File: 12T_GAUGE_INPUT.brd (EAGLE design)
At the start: 160 x 100 mm, 102 parts, among them J1 MICRO-SD_CARD_SOCKET, P1_WP_PULLUP 10k, P2_WP_PULLUP 10k, P3_WP_PULLUP 10k, U15 WS2812

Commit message: Routed board
Not optimized for size. This is a POC to get an idea of what the minimum size of the board can be
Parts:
- removed 3V-R1: 240, rcl:R1206
- removed 3V-R2: 390, rcl:R1206
- removed 3V3-DCPL: 10uF, rcl:C1206
- removed 3VREG: V_REG_317SMD, SparkFun-IC-Power:SOT223
- removed U15: WS2812, SparkFun-LED:LED-TRICOLOR-5050-IC
- added CAL12: WS2812, SparkFun-LED:LED-TRICOLOR-5050-IC
- added RTC_DCPL: 22uF, rcl:C1206
- moved CAL4 173.5 mm to (74.9, 11.4)
- moved B3-R1 166.0 mm to (58.4, 7.62), flipped to the bottom, turned to 90 degrees
- moved GAUGE2 163.2 mm to (47.0, 2.54)
- moved ADS2 156.8 mm to (69.8, 43.2), flipped to the bottom, turned to 270 degrees
- moved B7-R2 156.4 mm to (74.9, 53.3), flipped to the bottom, turned to 270 degrees
- moved B8-R2 156.4 mm to (59.7, 53.3), flipped to the bottom, turned to 270 degrees
- moved ADS2-DCPL2 155.7 mm to (61.0, 41.9), flipped to the bottom
- moved GAUGE6 154.0 mm to (90.2, 39.4), turned to 270 degrees
- moved B8-R1 153.9 mm to (64.8, 53.3), flipped to the bottom, turned to 270 degrees
- moved B6-R2 152.8 mm to (83.8, 41.9), flipped to the bottom, turned to 180 degrees
- moved B7-R1 152.7 mm to (78.7, 53.3), flipped to the bottom, turned to 270 degrees
- moved CAL3 152.0 mm to (61.0, 11.4)
- moved POT1-DCPL 151.0 mm to (58.4, 30.5)
- moved B2-R2 150.0 mm to (48.3, 7.62), flipped to the bottom, turned to 90 degrees
- moved GAUGE5 149.4 mm to (90.2, 25.4), turned to 270 degrees
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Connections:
- removed net +3V3: 3V-R1.2, 3V3-DCPL.1, 3VREG.2
- removed net N$8: 3V-R1.1, 3V-R2.2, 3VREG.1
- net +12V: no longer 3VREG.3
- net +5V: now also CAL12.3, CAL12.5, RTC_DCPL.1; no longer U15.3, U15.5
- net GND: now also CAL12.6, RTC_DCPL.2; no longer 3V-R2.1, 3V3-DCPL.2, U15.6
- net N$17: now also CAL12.2; no longer U15.2
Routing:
- net +5V: track 0.00 -> 558.2 mm, vias 0 -> 17
- net GND: track 0.00 -> 496.4 mm, vias 0 -> 31
- net AGND: track 0.00 -> 439.3 mm, vias 0 -> 10
- net V+: track 0.00 -> 362.9 mm, vias 0 -> 3
- net MOSI: track 0.00 -> 194.9 mm, vias 0 -> 10
- net SCK: track 0.00 -> 157.5 mm, vias 0 -> 8
- net WP: track 0.00 -> 154.1 mm, vias 0 -> 18
- net POT_SELECT_1: track 0.00 -> 150.1 mm, vias 0 -> 11
- net MISO: track 0.00 -> 141.7 mm, vias 0 -> 7
- net VREF: track 0.00 -> 140.0 mm, vias 0 -> 12
- net SCL: track 0.00 -> 139.3 mm, vias 0 -> 10
- net SDA: track 0.00 -> 124.8 mm, vias 0 -> 12
- net POT_SELECT_0: track 0.00 -> 112.3 mm, vias 0 -> 10
- net ADS_SYNC: track 0.00 -> 112.0 mm, vias 0 -> 15
- net XTAL2: track 0.00 -> 107.4 mm, vias 0 -> 13
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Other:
- board size 160 x 100 mm -> 94 x 61.9 mm

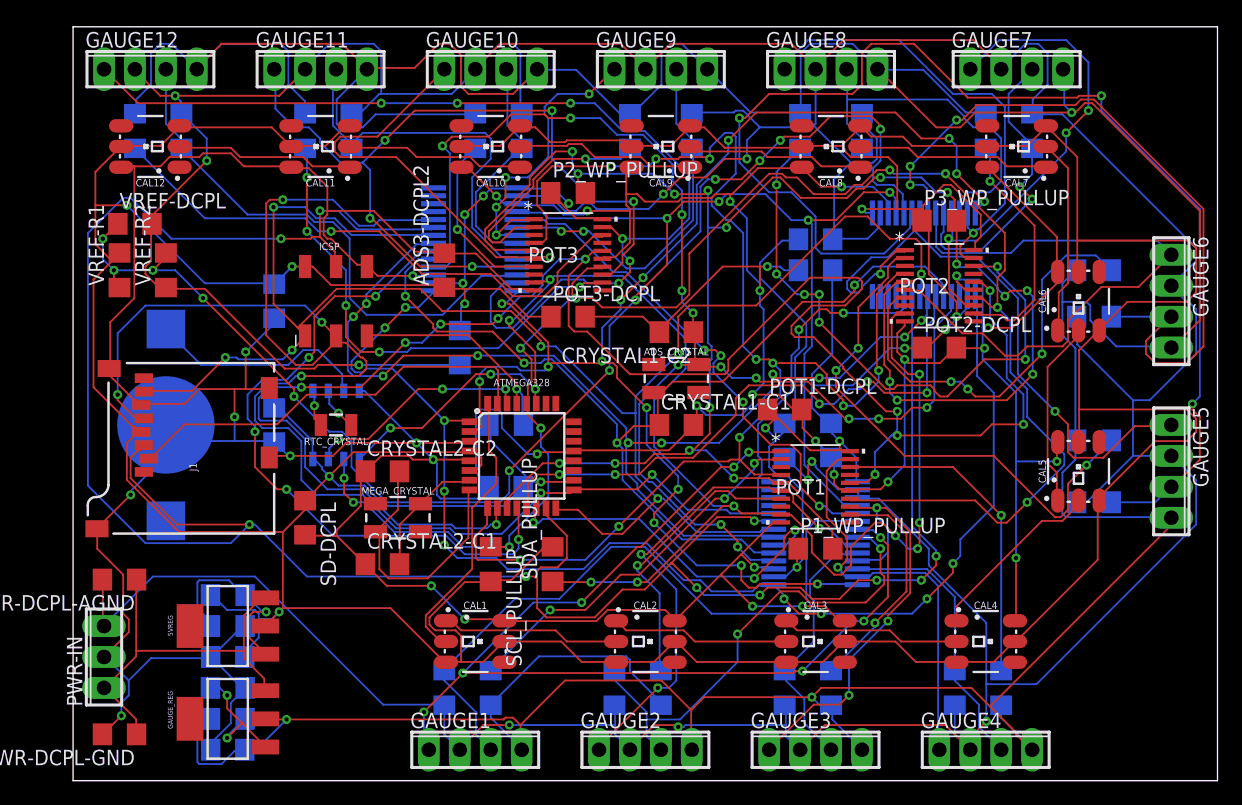
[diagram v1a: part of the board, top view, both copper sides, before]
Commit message: First size optimization
3.75x2.5 down to 3.5x2.5
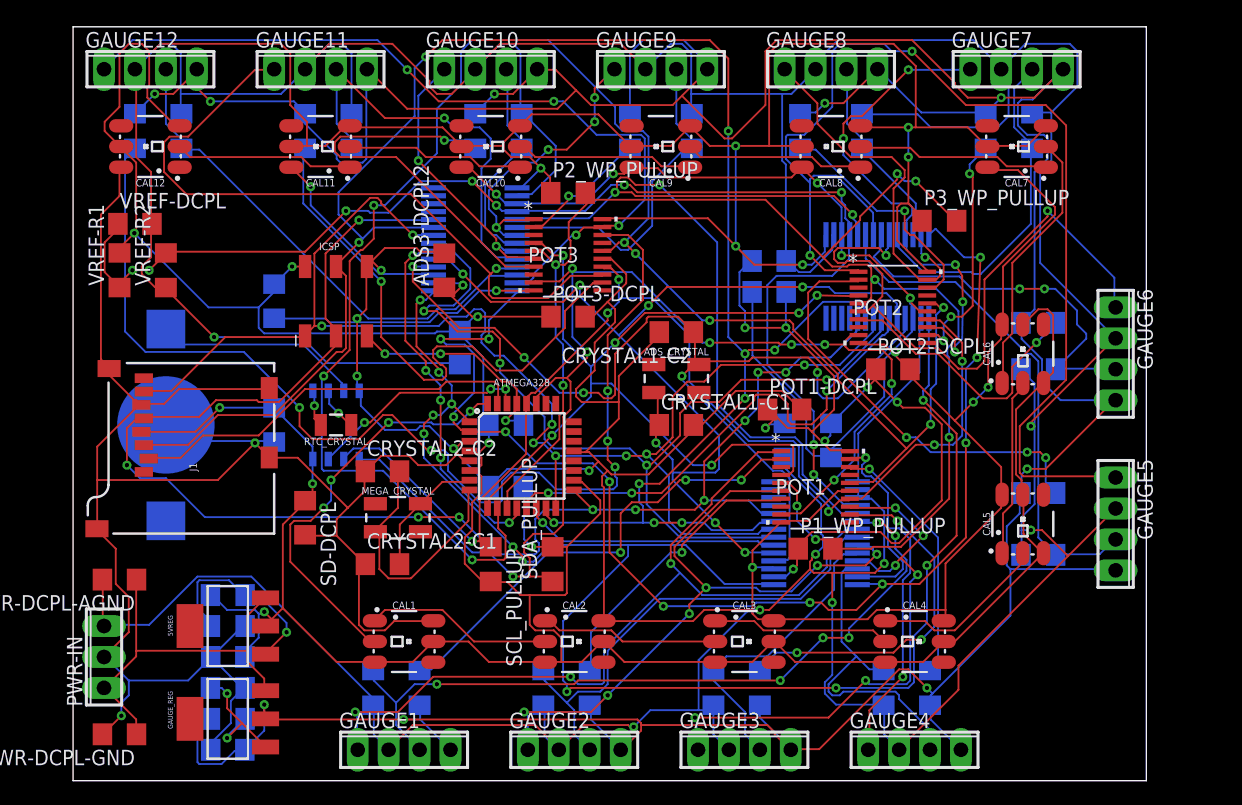
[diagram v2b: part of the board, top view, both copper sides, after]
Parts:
- RTC_DCPL: value 22uF -> 10uF
- moved CAL5 6.29 mm to (78.0, 21.1)
- moved CAL6 6.29 mm to (78.0, 35.1)
- moved GAUGE5 6.29 mm to (85.6, 21.1)
- moved GAUGE6 6.29 mm to (85.6, 35.1)
- moved B6-R1 6.29 mm to (79.2, 33.8)
- moved B5-R2 6.29 mm to (79.2, 23.6)
- moved B5-R1 6.29 mm to (79.2, 18.5)
- moved B6-R2 6.29 mm to (79.2, 37.6)
- moved CAL4 5.84 mm to (69.1, 11.4)
- moved GAUGE4 5.84 mm to (69.1, 2.54)
- moved B2-R1 5.84 mm to (38.6, 7.62)
- moved CAL1 5.84 mm to (27.2, 11.4)
- moved GAUGE1 5.84 mm to (27.2, 2.54)
- moved B1-R1 5.84 mm to (24.6, 7.62)
- moved B1-R2 5.84 mm to (28.4, 7.62)
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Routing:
- net B5+: track 102.6 -> 41.6 mm, vias 3 -> 0
- net P3B3: track 46.1 -> 92.2 mm, vias 1 -> 5
- net B5-_P2W0: track 51.2 -> 93.6 mm
- net SCL: track 139.3 -> 97.5 mm, vias 10 -> 6
- net MOSI: track 194.9 -> 157.4 mm
- net POT_SELECT_0: track 112.3 -> 75.8 mm, vias 10 -> 6
- net V+: track 362.9 -> 326.5 mm, vias 3 -> 9
- net VREF: track 140.0 -> 107.0 mm, vias 12 -> 9
- net WP: track 154.1 -> 121.2 mm, vias 18 -> 8
- net SCK: track 157.5 -> 126.7 mm, vias 8 -> 10
- net P2B3: track 49.2 -> 19.5 mm, vias 7 -> 1
- net B6+: track 60.9 -> 31.7 mm, vias 3 -> 2
- net ADS3_CS: track 56.2 -> 29.7 mm
- net ADS_RESET: track 104.4 -> 129.4 mm, vias 9 -> 11
- net XTAL2: track 107.4 -> 83.9 mm, vias 13 -> 5
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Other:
- board size 94 x 61.9 mm -> 88.1 x 61.9 mm

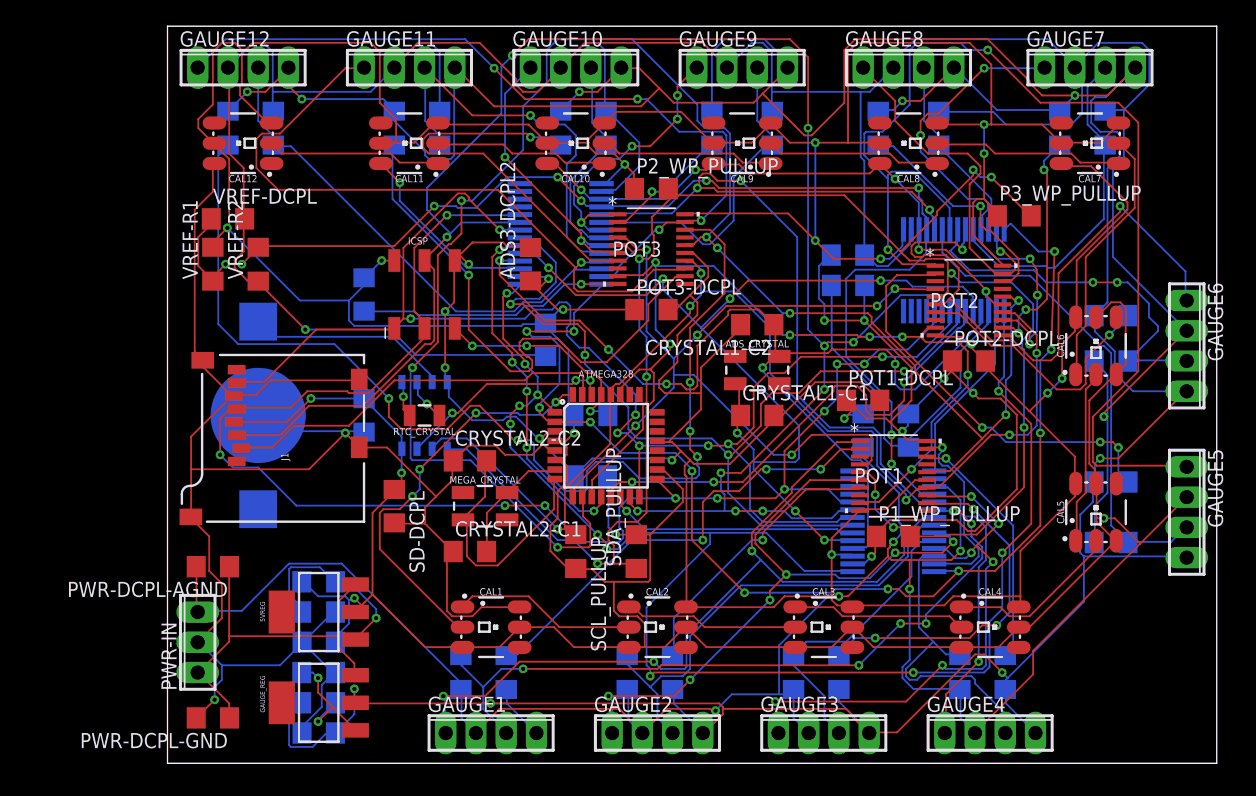
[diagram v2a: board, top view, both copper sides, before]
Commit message: Size optimization round 2
Down to 3.1x2.5
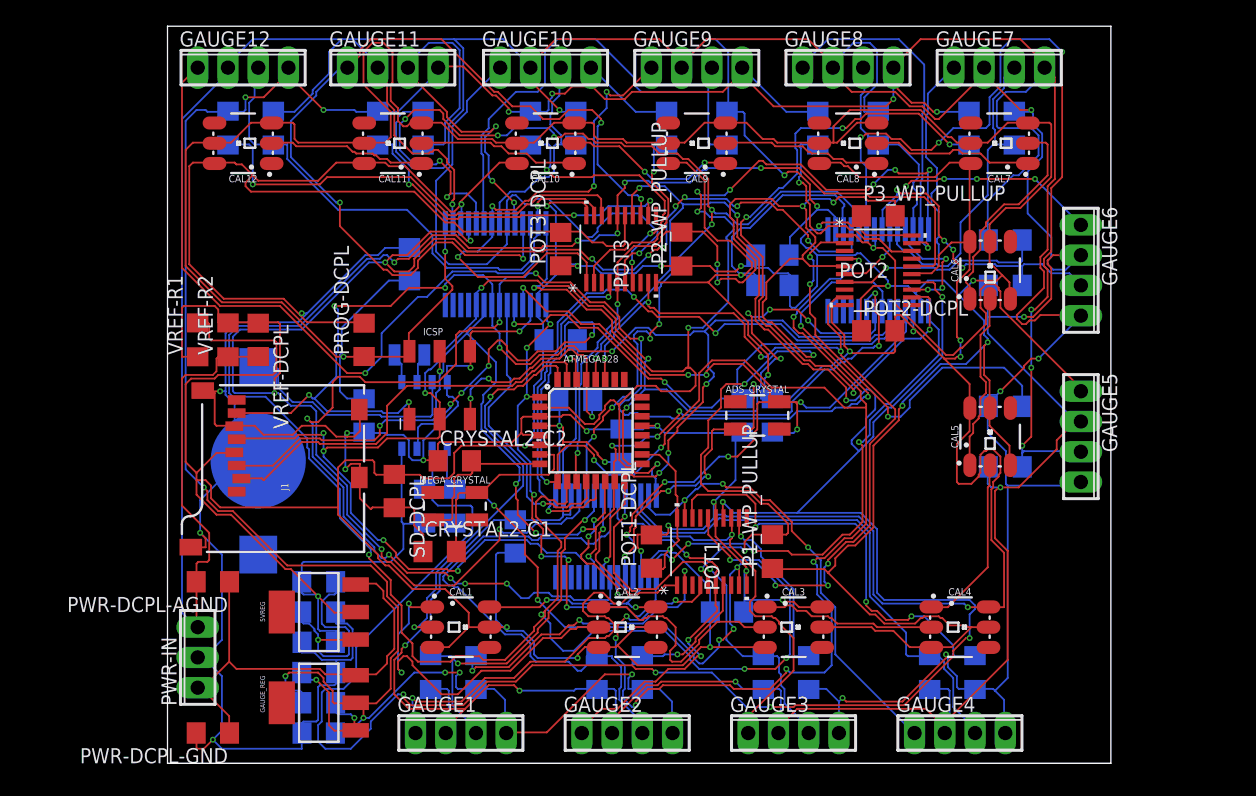
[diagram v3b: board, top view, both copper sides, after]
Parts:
- moved ADS1-DCPL1 30.5 mm to (29.2, 19.1), turned to 90 degrees
- moved ADS1 24.2 mm to (36.8, 19.1), turned to 270 degrees
- moved POT1-DCPL 21.8 mm to (40.6, 17.8), turned to 90 degrees
- moved ADS1-DCPL2 21.6 mm to (47.0, 12.7), turned to 180 degrees
- moved POT1 16.5 mm to (45.7, 17.8), turned to 90 degrees
- moved SDA_PULLUP 15.7 mm to (24.1, 21.6), flipped to the bottom, turned to 270 degrees
- moved SCL_PULLUP 13.3 mm to (21.6, 21.6), flipped to the bottom
- moved P3_WP_PULLUP 11.4 mm to (59.7, 46.0)
- moved B5-R2 10.9 mm to (70.4, 30.0)
- moved B6-R1 10.9 mm to (70.4, 40.1)
- moved B6-R2 10.9 mm to (70.4, 43.9)
- moved CAL6 10.9 mm to (69.1, 41.4)
- moved GAUGE6 10.9 mm to (76.7, 41.4)
- moved B5-R1 10.9 mm to (70.4, 24.9)
- moved CAL5 10.9 mm to (69.1, 27.4)
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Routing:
- net SCL: track 97.5 -> 216.7 mm, vias 6 -> 10
- net POT_SELECT_0: track 75.8 -> 138.4 mm, vias 6 -> 12
- net B5-_P2W0: track 93.6 -> 37.4 mm, vias 2 -> 1
- net MOSI: track 157.4 -> 103.3 mm, vias 10 -> 11
- net P3B3: track 92.2 -> 38.4 mm, vias 5 -> 1
- net ADS_DRDY: track 77.1 -> 126.7 mm, vias 4 -> 10
- net ADS_RESET: track 129.4 -> 84.0 mm
- net +5V: track 540.6 -> 585.6 mm, vias 22 -> 19
- net P2B2: track 19.5 -> 58.8 mm, vias 3 -> 5
- net VREF: track 107.0 -> 145.9 mm, vias 9 -> 12
- net POT_SELECT_1: track 144.5 -> 182.9 mm, vias 8 -> 10
- net GND: track 497.0 -> 532.8 mm, vias 18 -> 26
- net B5+: track 41.6 -> 74.7 mm, vias 0 -> 6
- net V+: track 326.5 -> 359.1 mm, vias 9 -> 16
- net B1+: track 61.9 -> 31.1 mm, vias 6 -> 2
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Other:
- board size 88.1 x 61.9 mm -> 79.2 x 61.9 mm

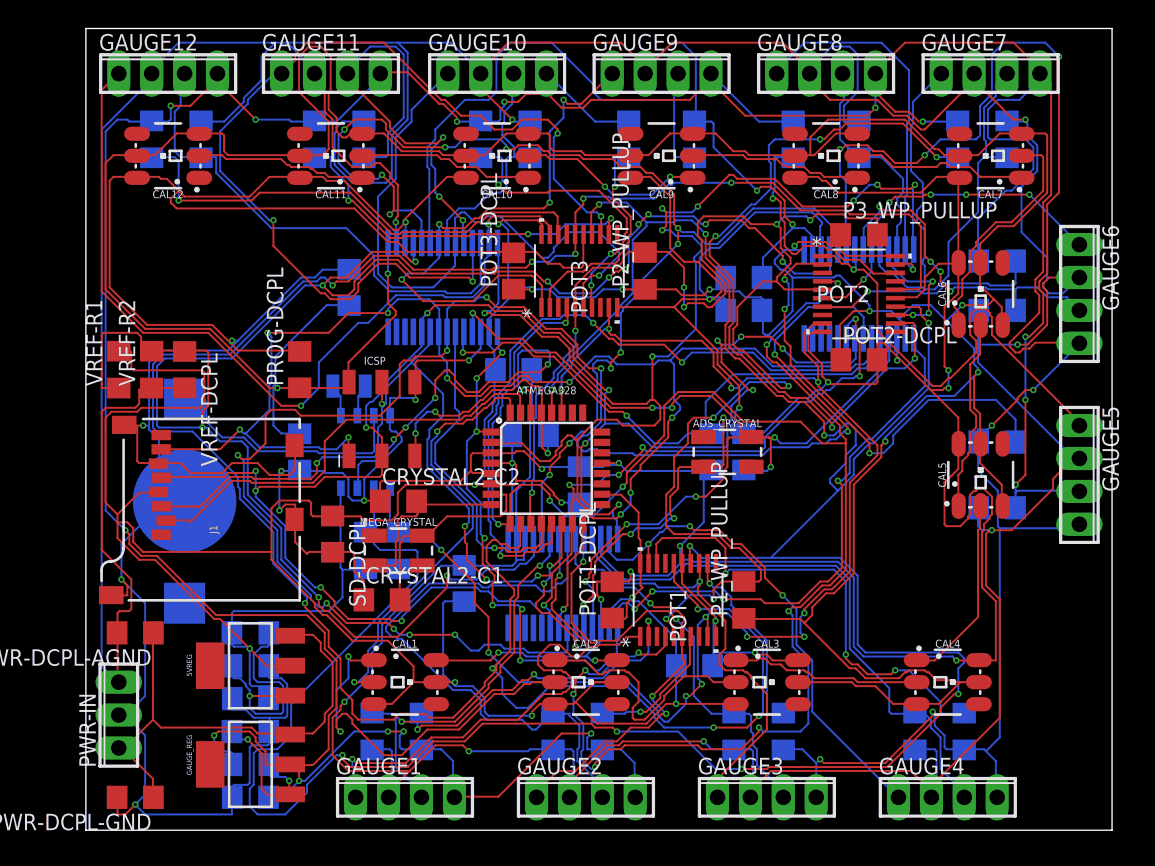
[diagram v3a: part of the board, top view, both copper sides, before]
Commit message: Size optimization V3
THERE IS A MISSING CONNECTION! THIS IS ONLY A PROGRESS UPDATE
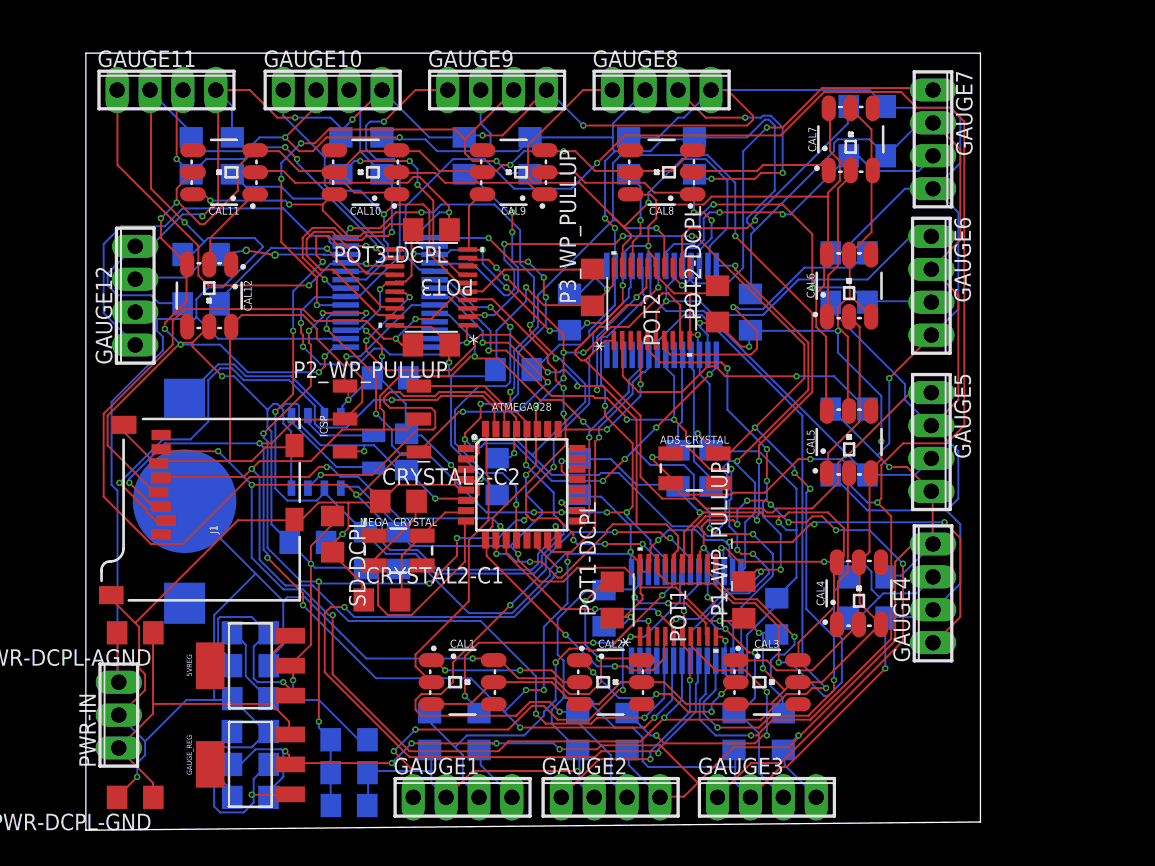
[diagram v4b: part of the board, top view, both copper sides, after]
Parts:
- moved VREF-DCPL 36.0 mm to (20.3, 1.91), flipped to the bottom, turned to 180 degrees
- moved VREF-R2 34.6 mm to (20.3, 4.45), flipped to the bottom, turned to 0 degrees
- moved VREF-R1 33.7 mm to (20.3, 6.99), flipped to the bottom, turned to 180 degrees
- moved P3_WP_PULLUP 21.0 mm to (39.1, 41.9), turned to 90 degrees
- moved P2_WP_PULLUP 17.5 mm to (26.7, 37.5), turned to 180 degrees
- moved GAUGE12 17.3 mm to (3.81, 41.3), turned to 90 degrees
- moved POT2 16.0 mm to (43.7, 40.6), turned to 90 degrees
- moved GAUGE4 15.8 mm to (65.4, 18.3), turned to 90 degrees
- moved ADS2 15.3 mm to (44.5, 40.1)
- moved B4-R2 14.1 mm to (60.3, 19.6), turned to 0 degrees
- moved ADS2-DCPL2 13.5 mm to (37.3, 40.0), turned to 270 degrees
- moved B11-R1 13.4 mm to (8.13, 52.1)
- moved B12-R2 13.3 mm to (8.89, 40.6), turned to 180 degrees
- moved B8-R2 12.8 mm to (41.9, 52.1)
- moved B9-R1 12.8 mm to (34.3, 52.1)
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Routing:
- net +5V: track 585.6 -> 428.6 mm, vias 19 -> 28
- net GND: track 532.8 -> 416.4 mm, vias 26 -> 24
- net POT_SELECT_1: track 182.9 -> 72.5 mm, vias 10 -> 8
- net AGND: track 459.7 -> 363.4 mm, vias 10 -> 7
- net V+: track 359.1 -> 266.7 mm, vias 16 -> 13
- net XTAL1: track 70.3 -> 156.5 mm, vias 6 -> 5
- net POT_SELECT_0: track 138.4 -> 57.5 mm, vias 12 -> 6
- net ADS_DRDY: track 126.7 -> 55.9 mm, vias 10 -> 6
- net SCL: track 216.7 -> 146.1 mm, vias 10 -> 9
- net MISO: track 110.3 -> 173.3 mm
- net ADS2_CS: track 56.1 -> 0.00 mm, vias 3 -> 0
- net ADS1_CS: track 13.6 -> 64.9 mm
- net B5+: track 74.7 -> 30.3 mm, vias 6 -> 0
- net VREF: track 145.9 -> 103.0 mm, vias 12 -> 13
- net B11-_P3W2: track 75.8 -> 33.2 mm, vias 4 -> 2
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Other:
- board size 79.2 x 61.9 mm -> 69.1 x 60 mm
